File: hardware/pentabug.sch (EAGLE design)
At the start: 15 parts, among them IC1 ATMEGA88

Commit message: some routing
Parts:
- removed SG2: BUZZERPTH, SparkFun:BUZZERPTH
- added SG1: MULTIBUZZR, buglbr:MULTIBUZZR
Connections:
- net BUZZR: now also SG1.+; no longer SG2.1
- net GND: now also SG1.-; no longer SG2.2
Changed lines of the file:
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@@
 <part name="GND11" library="supply1" deviceset="GND" device=""/>
 <part name="Q1" library="transistors" deviceset="2N700*" device="_TO92" technology="0"/>
-<part name="SG2" library="SparkFun" deviceset="BUZZER" device="PTH"/>
 <part name="R3" library="rcl" deviceset="R-EU_" device="0207/10" value="10k"/>
 <part name="LED1" library="SparkFun" deviceset="LED" device="5MM"/>
@@
 <part name="JP2" library="pinhead" deviceset="PINHD-2X3" device=""/>
 <part name="U$1" library="buglbr" deviceset="VIBRAMOTOR" device=""/>
+<part name="SG1" library="buglbr" deviceset="MULTIBUZZR" device=""/>
 </parts>
 <sheets>
@@
 <instance part="GND11" gate="1" x="2.54" y="25.4" smashed="yes"/>
 <instance part="Q1" gate="G$1" x="116.84" y="20.32"/>
-<instance part="SG2" gate="G$1" x="93.98" y="-2.54" rot="R270"/>
 <instance part="R3" gate="G$1" x="-5.08" y="76.2" rot="R180"/>
 <instance part="LED1" gate="G$1" x="71.12" y="76.2" smashed="yes" rot="R90">
@@
 <instance part="JP2" gate="A" x="180.34" y="83.82"/>
 <instance part="U$1" gate="G$1" x="139.7" y="38.1"/>
+<instance part="SG1" gate="G$1" x="96.52" y="0" rot="R270"/>
 </instances>
 <busses>
@@
 </segment>
 <segment>
-<wire x1="86.36" y1="-5.08" x2="91.44" y2="-5.08" width="0.1524" layer="91"/>
-<pinref part="SG2" gate="G$1" pin="2"/>
+<wire x1="86.36" y1="-5.08" x2="93.98" y2="-5.08" width="0.1524" layer="91"/>
 <pinref part="GND3" gate="1" pin="GND"/>
+<pinref part="SG1" gate="G$1" pin="-"/>
 </segment>
 <segment>
@@
 <net name="BUZZR" class="0">
 <segment>
-<wire x1="91.44" y1="-2.54" x2="76.2" y2="-2.54" width="0.1524" layer="91"/>
-<label x="78.74" y="-2.54" size="1.778" layer="95"/>
-<pinref part="SG2" gate="G$1" pin="1"/>
-</segment>
-<segment>
+<wire x1="93.98" y1="2.54" x2="86.36" y2="2.54" width="0.1524" layer="91"/>
+<label x="81.28" y="2.54" size="1.778" layer="95"/>
+<pinref part="SG1" gate="G$1" pin="+"/>
+</segment>
+<segment>

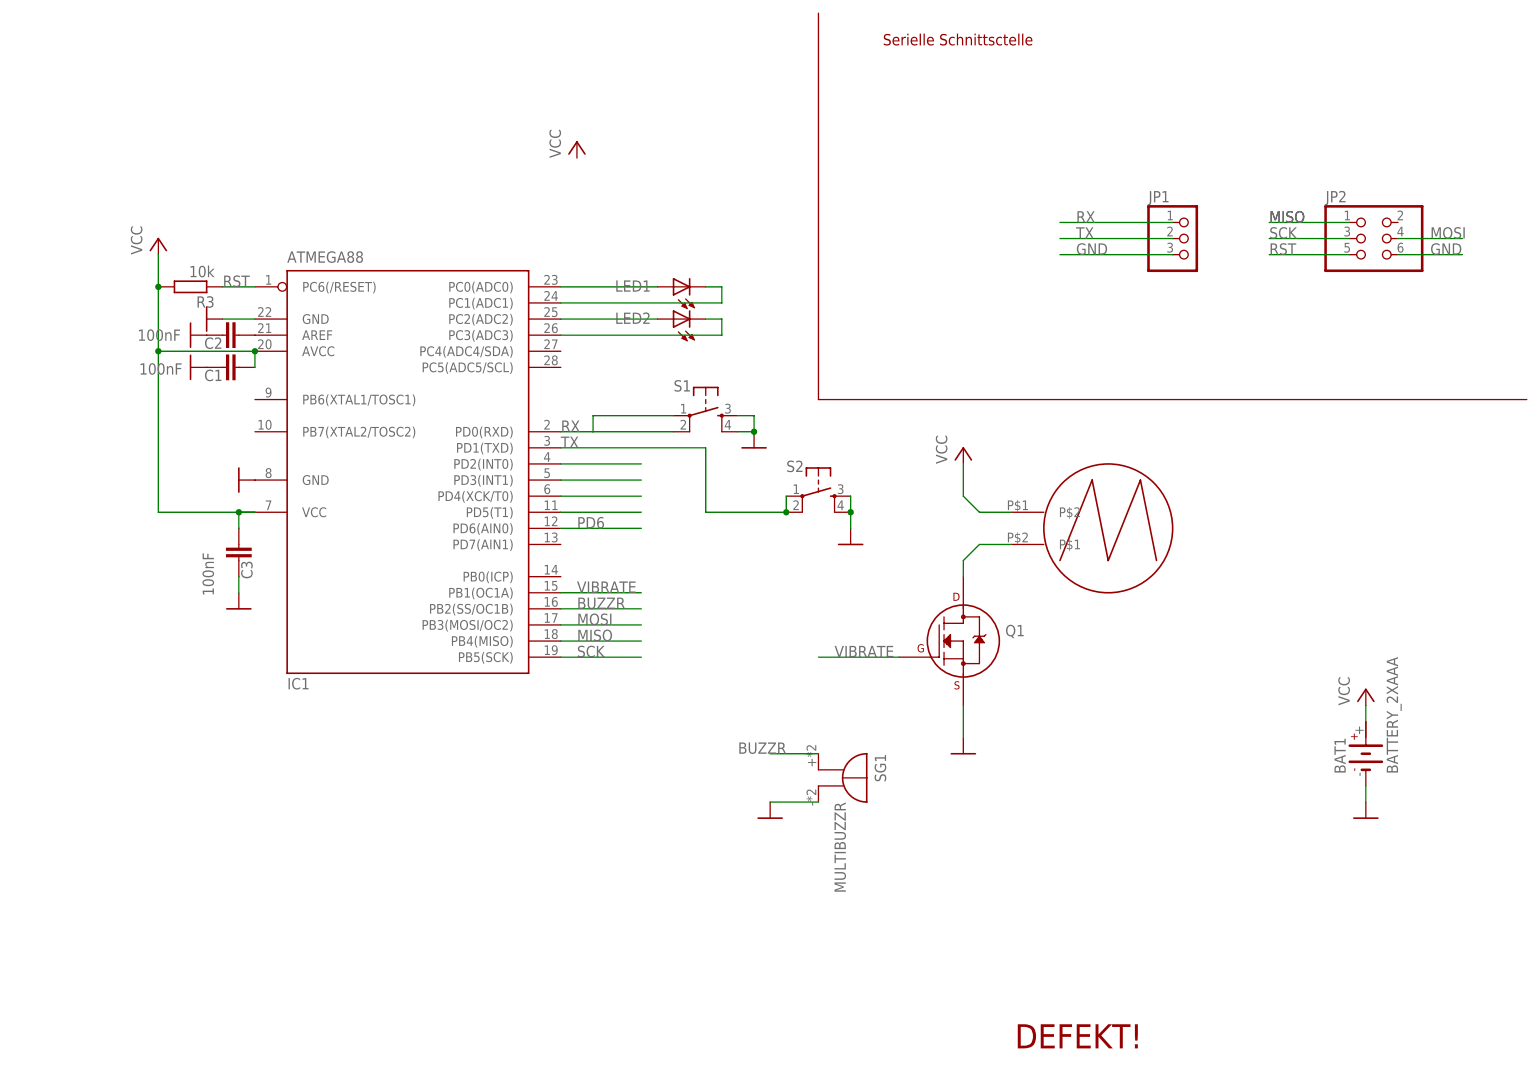
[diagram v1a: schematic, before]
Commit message: Lots of routing done, GND from Buzzer connected to ADC6 for measurement
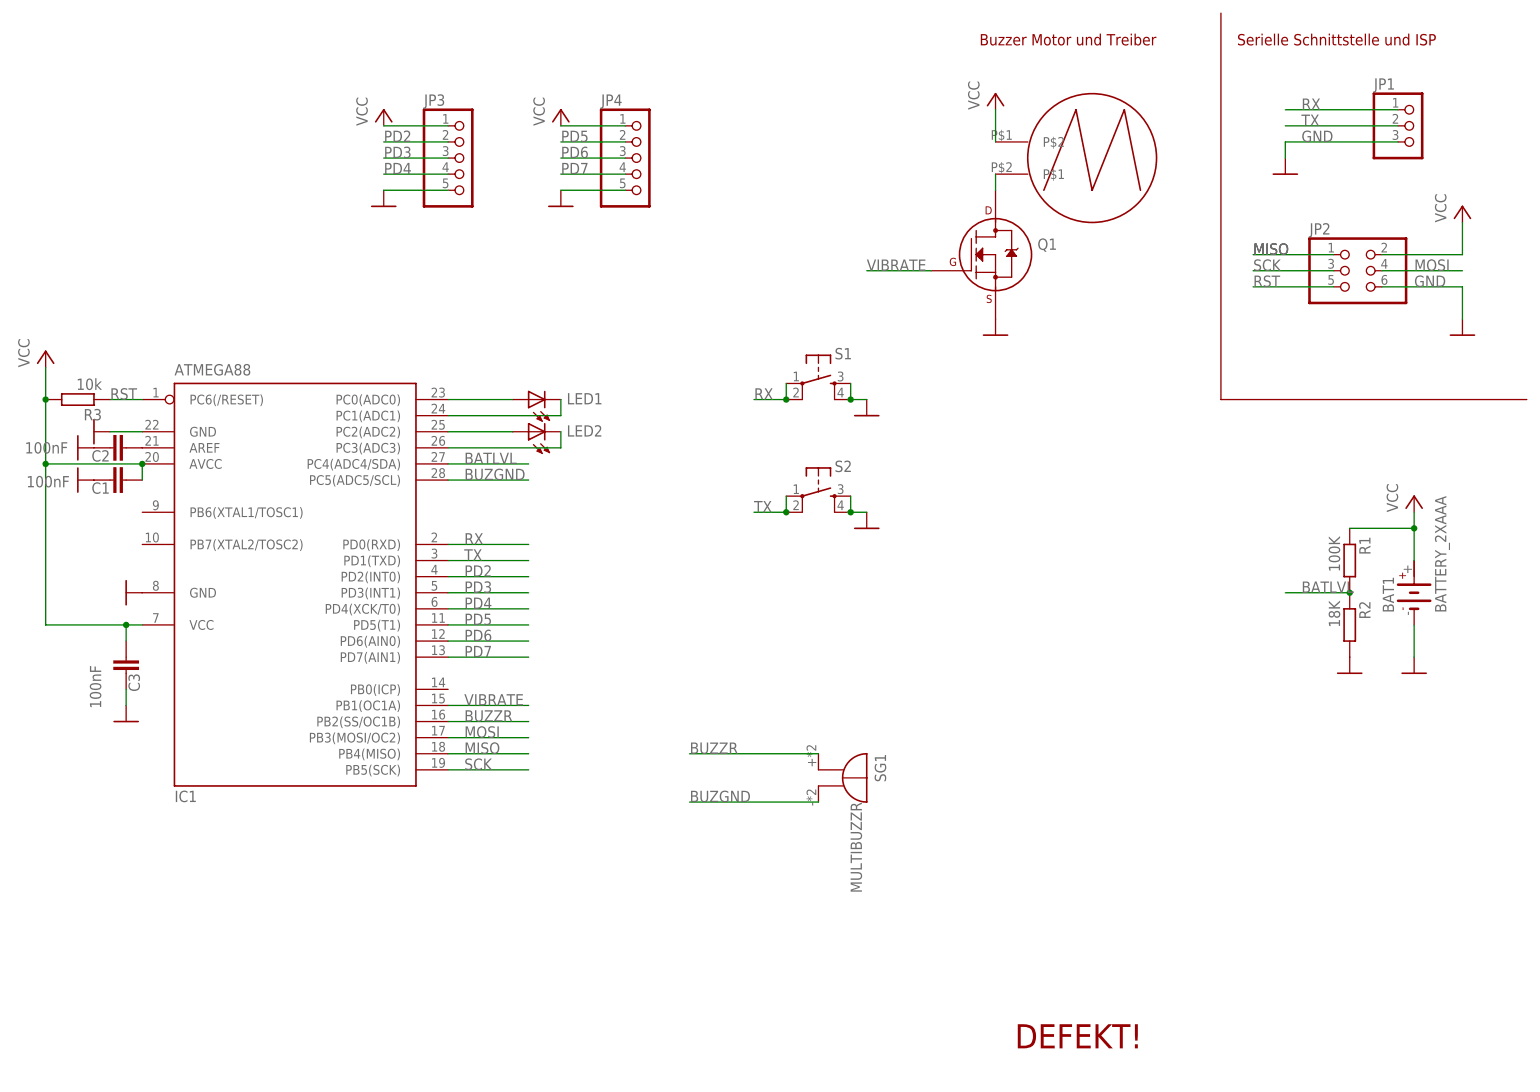
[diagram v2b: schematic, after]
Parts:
- added JP3, JP4: (no value), pinhead:PINHD-1X5
- added R1: 100K, rcl:R-EU_0207/10
- added R2: 18K, rcl:R-EU_0207/10
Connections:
- net N$11 renamed BATTLVL
- removed net N$22: IC1.PD4(XCK/T0)
- removed net N$4: IC1.PD2(INT0)
- removed net N$7: IC1.PD5(T1)
- removed net N$9: IC1.PD3(INT1)
- new net BATLVL: IC1.PC4(ADC4/SDA), R1.2, R2.1
- new net BUZGND: IC1.PC5(ADC5/SCL), SG1.-
- new net PD2: IC1.PD2(INT0), JP3.2
- new net PD3: IC1.PD3(INT1), JP3.3
- new net PD4: IC1.PD4(XCK/T0), JP3.4
- new net PD5: IC1.PD5(T1), JP4.2
- new net PD7: IC1.PD7(AIN1), JP4.4
- net GND: now also JP3.5, JP4.5, R2.2; no longer SG1.-
- net PD6: now also JP4.3
- net VCC: now also JP2.2, JP3.1, JP4.1, R1.1
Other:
- note added: "Buzzer Motor und Treiber"
- note added: "Serielle Schnittstelle und ISP"
- note removed: "Serielle Schnittsctelle"
- moved on the sheet: BAT1, C1, C2, C3, IC1, JP1, JP2, LED1, LED2, Q1, R3, S1

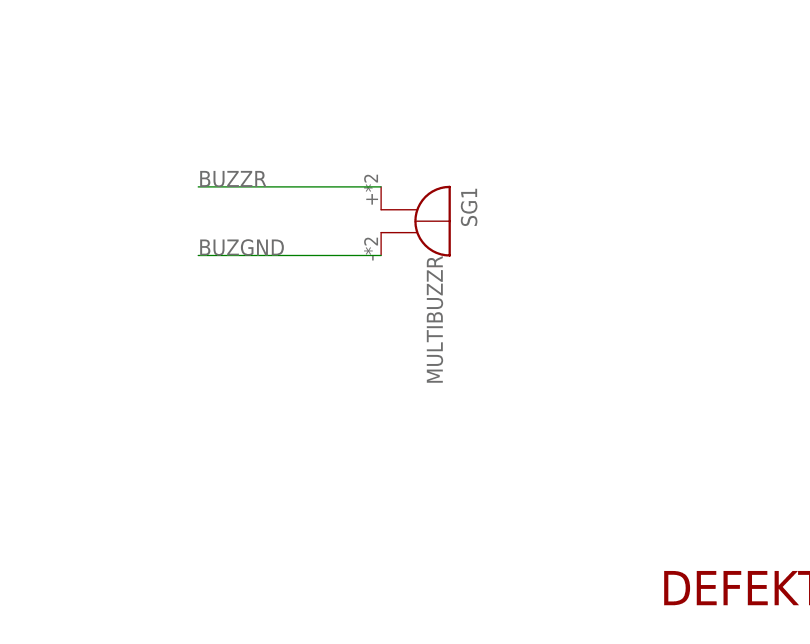
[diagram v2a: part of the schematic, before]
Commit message: modified to use biggr buzzr - routing not adapted yet!
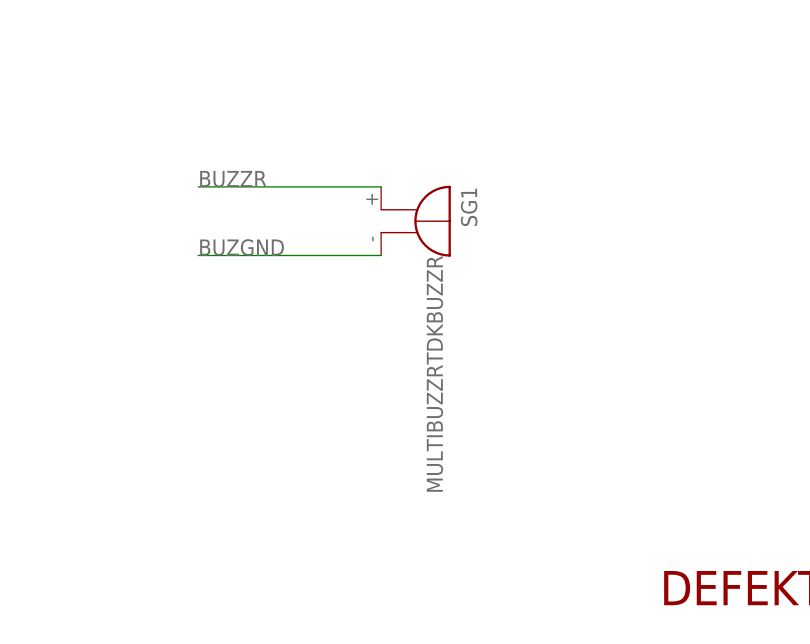
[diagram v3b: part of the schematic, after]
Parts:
- SG1: value MULTIBUZZR -> MULTIBUZZRTDKBUZZR; device buglbr:MULTIBUZZR -> buglbr:MULTIBUZZRTDKBUZZR
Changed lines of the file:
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@@
 <part name="JP2" library="pinhead" deviceset="PINHD-2X3" device=""/>
 <part name="U$1" library="buglbr" deviceset="VIBRAMOTOR" device=""/>
-<part name="SG1" library="buglbr" deviceset="MULTIBUZZR" device=""/>
+<part name="SG1" library="buglbr" deviceset="MULTIBUZZR" device="TDKBUZZR"/>
 <part name="GND10" library="supply1" deviceset="GND" device=""/>
 <part name="GND12" library="supply1" deviceset="GND" device=""/>

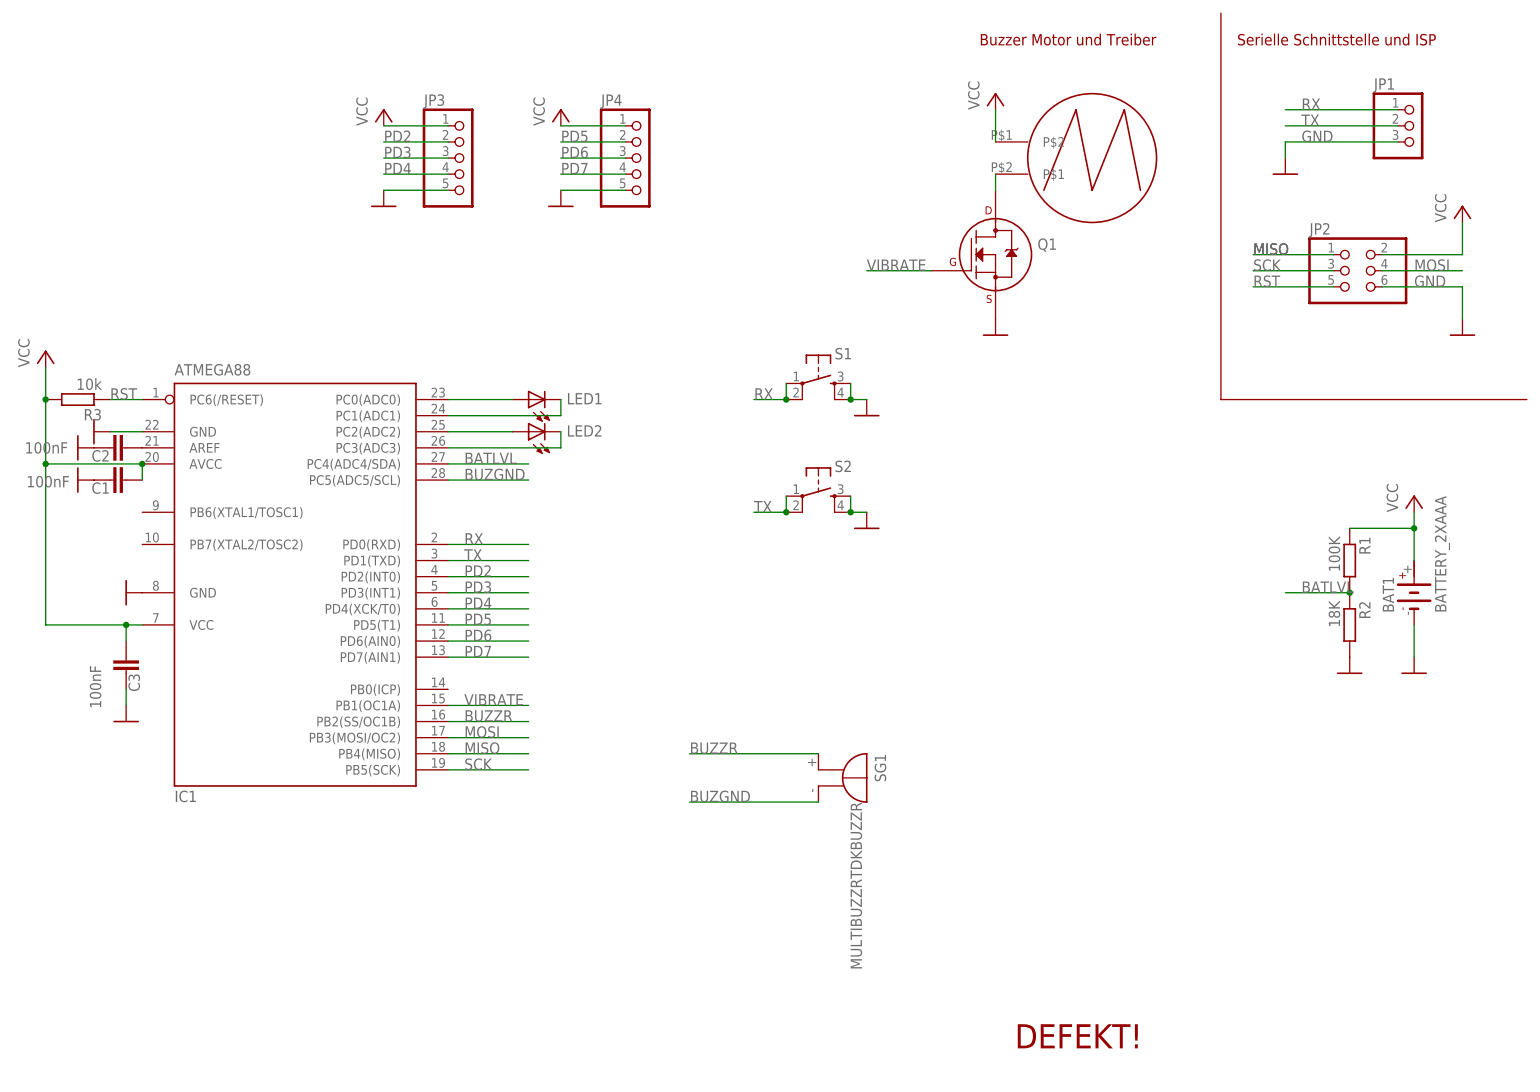
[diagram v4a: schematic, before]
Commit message: some schematics beautification
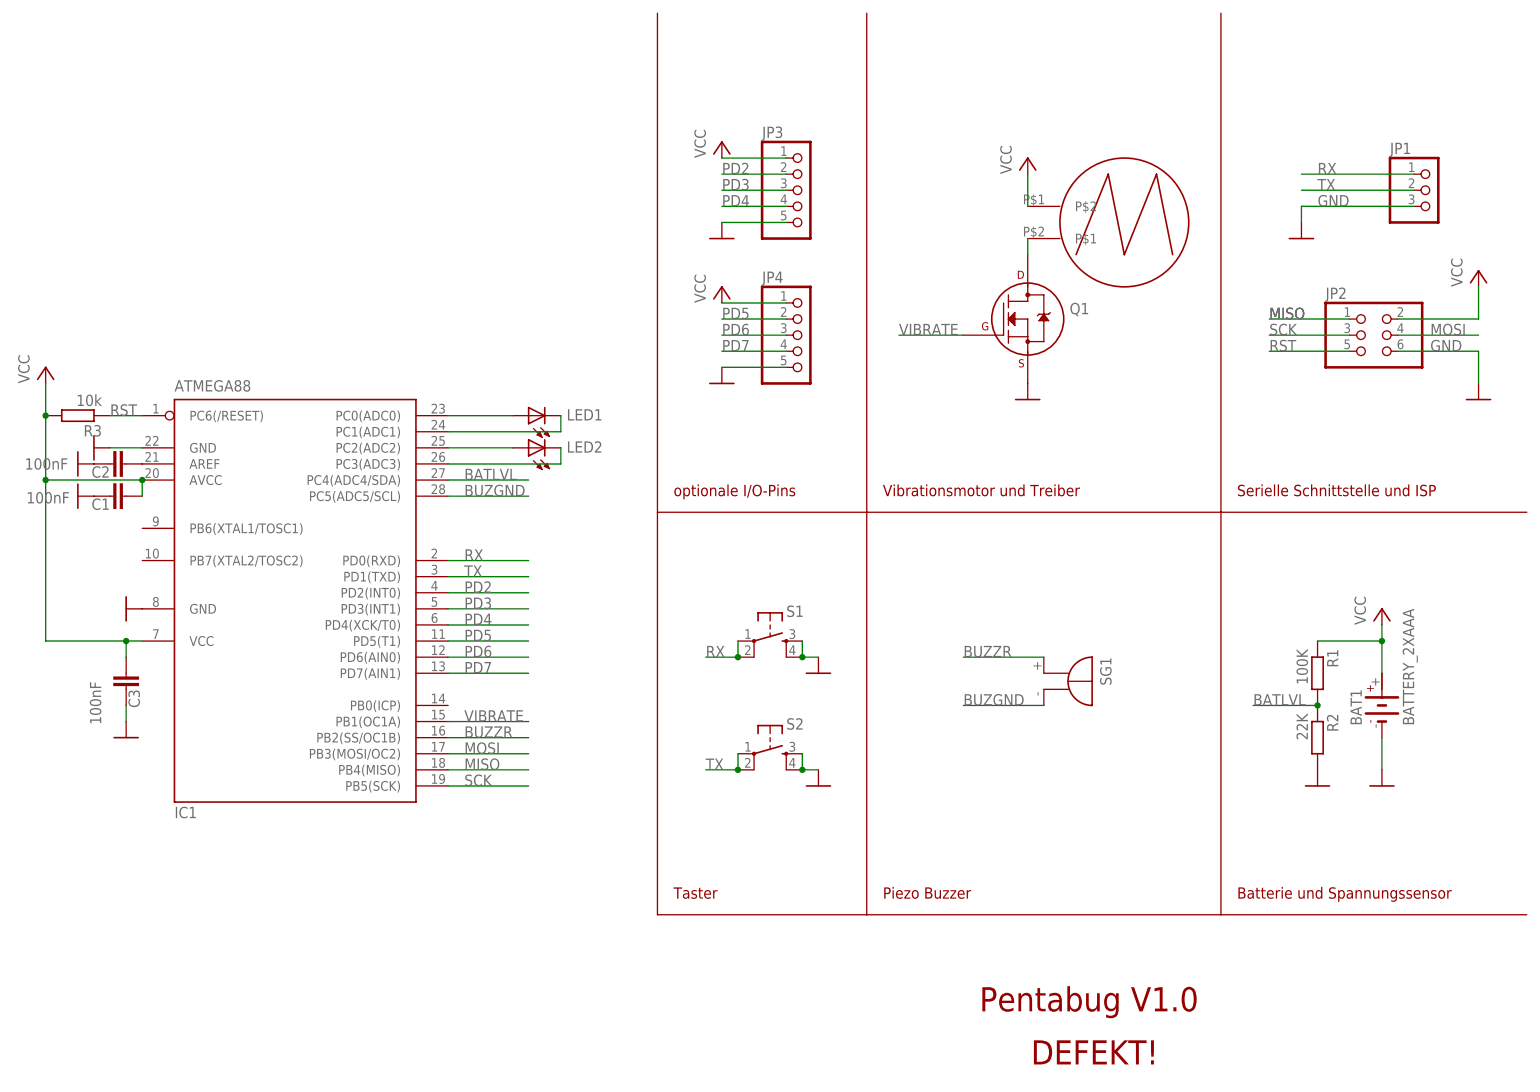
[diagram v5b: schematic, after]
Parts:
- R2: value 18K -> 22K
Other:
- note added: "Batterie und Spannungssensor"
- note added: "Pentabug V1.0"
- note added: "Piezo Buzzer"
- note added: "Taster"
- note added: "Vibrationsmotor und Treiber"
- note added: "optionale I/O-Pins"
- note removed: "Buzzer Motor und Treiber"
- moved on the sheet: BAT1, C1, C2, C3, IC1, JP1, JP2, JP3, JP4, LED1, LED2, Q1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
